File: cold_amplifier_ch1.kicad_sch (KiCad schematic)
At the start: 28 parts, among them J2 T1M-03-F-SV-L, J3 T1M-03-F-SV-L, J4 T1M-03-F-SV-L, J5 T1M-03-F-SV-L

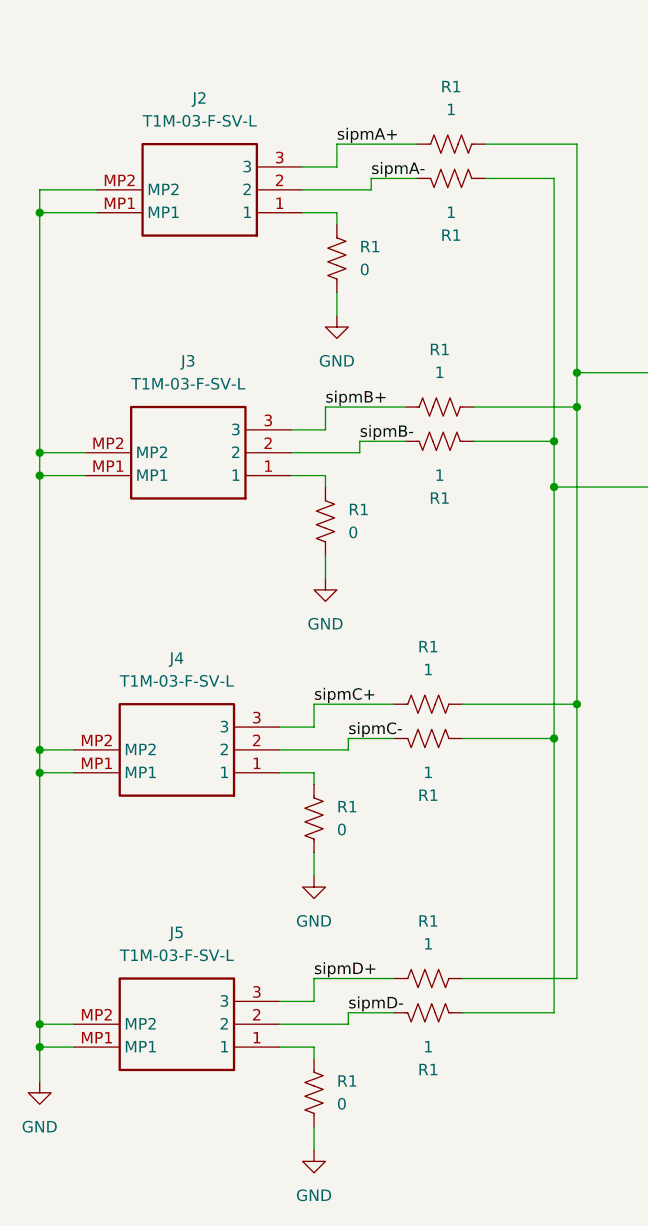
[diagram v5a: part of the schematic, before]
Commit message: Solved error in netlist; input connector was in a mirror configuration; solved also DB15 error in netlist
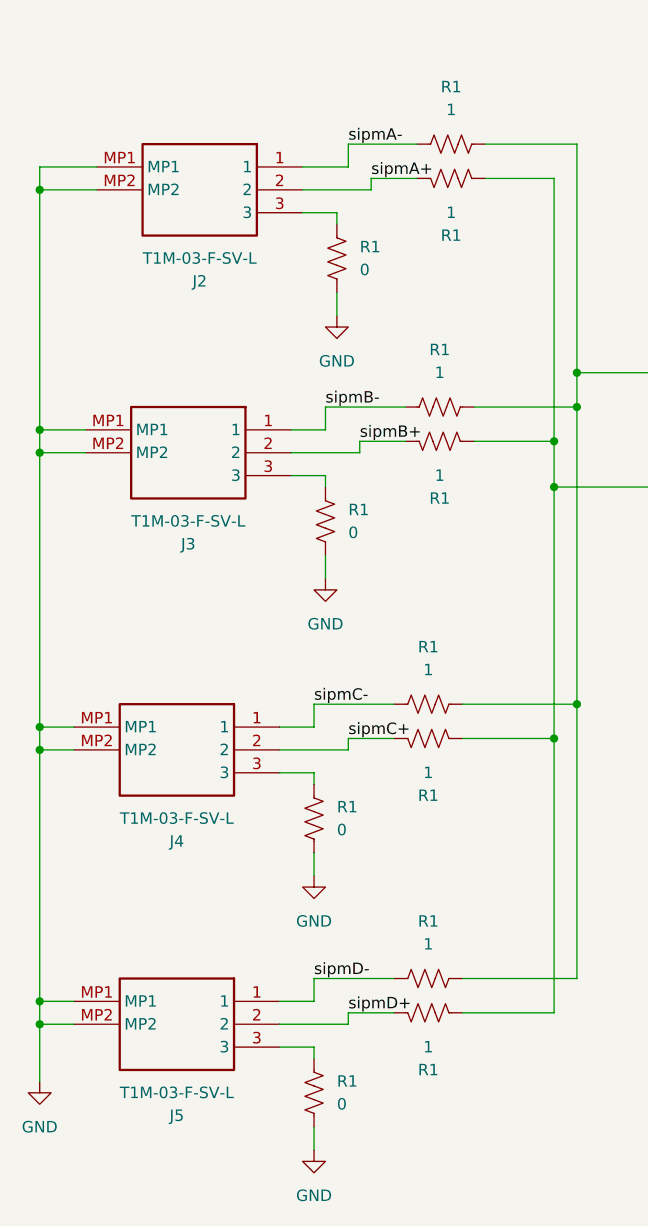
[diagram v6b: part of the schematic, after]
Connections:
- net sipmA+: now also J2.2, R1.2; no longer J2.3, R1.1
- net sipmA-: now also J2.1, R1.1; no longer J2.2, R1.2
- net sipmB+: now also J3.2, R1.2; no longer J3.3, R1.1
- net sipmB-: now also J3.1, R1.1; no longer J3.2, R1.2
- net sipmC+: now also J4.2, R1.2; no longer J4.3, R1.1
- net sipmC-: now also J4.1, R1.1; no longer J4.2, R1.2
- net sipmD+: now also J5.2, R1.2; no longer J5.3, R1.1
- net sipmD-: now also J5.1, R1.1; no longer J5.2, R1.2
- net at R1.2: now also J2.3; no longer J2.1
- net at R1.2: now also J5.3; no longer J5.1
- net at R1.2: now also J4.3; no longer J4.1
- net at R1.2: now also J3.3; no longer J3.1
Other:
- moved on the sheet: J2, J3, J4, J5

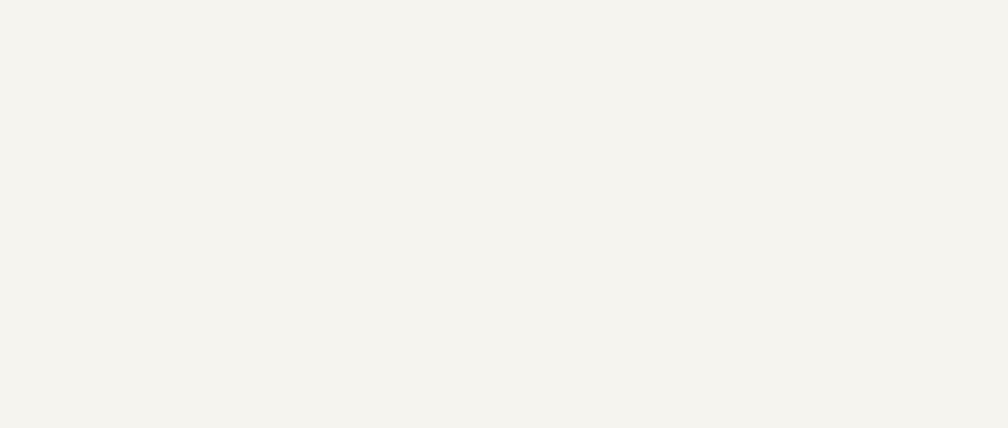
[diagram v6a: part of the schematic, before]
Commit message: Version tested at coldbox March 2026
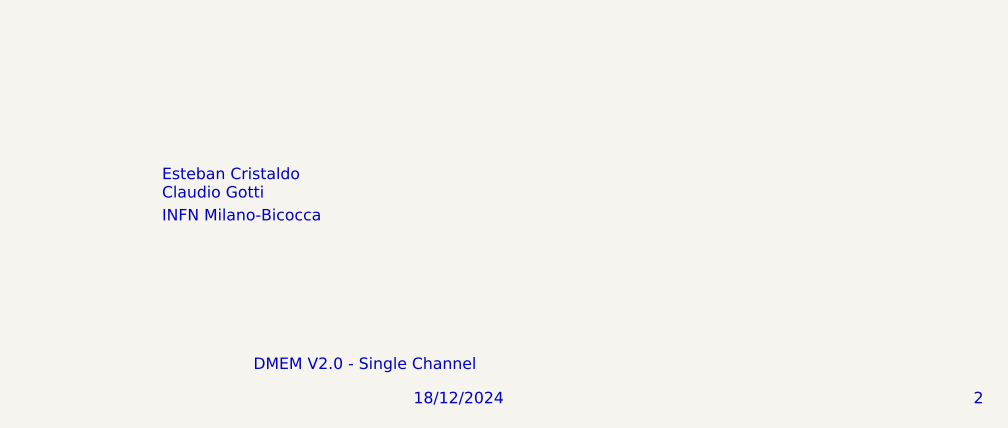
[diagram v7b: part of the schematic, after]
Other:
- note added: "18/12/2024"
- note added: "2"
- note added: "DMEM V2.0 - Single Channel"
- note added: "Esteban Cristaldo Claudio Gotti"
- note added: "INFN Milano-Bicocca"
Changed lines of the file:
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@@
     (stroke (width 0) (type default))
+  )
+  (text "2\n" (at 267.97 194.31 0)
+    (effects (font (size 1.27 1.27)) (justify left bottom))
+  )
+  (text "Esteban Cristaldo \nClaudio Gotti\n" (at 177.8 171.45 0)
+    (effects (font (size 1.27 1.27)) (justify left bottom))
+  )
+  (text "DMEM V2.0 - Single Channel" (at 187.96 190.5 0)
+    (effects (font (size 1.27 1.27)) (justify left bottom))
+  )
+  (text "18/12/2024\n" (at 205.74 194.31 0)
+    (effects (font (size 1.27 1.27)) (justify left bottom))
+  )
+  (text "INFN Milano-Bicocca\n" (at 177.8 173.99 0)
+    (effects (font (size 1.27 1.27)) (justify left bottom))
   )
   (label "input-" (at 97.79 91.44 0) (fields_autoplaced)
